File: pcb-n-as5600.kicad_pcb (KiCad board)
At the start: 2 copper layers, 41 x 35 mm, 26 parts, among them J1 Conn_01x04, J2 Conn_01x04_Pin, J5 Conn_01x04, J6 USB_C_Receptacle_USB2.0_14P, SW2 SW_Push, SW3 SW_Push, U4 AS5600, U5 STM32F103C8Tx, U6 AP2112K-3.3, Y2 8MHz

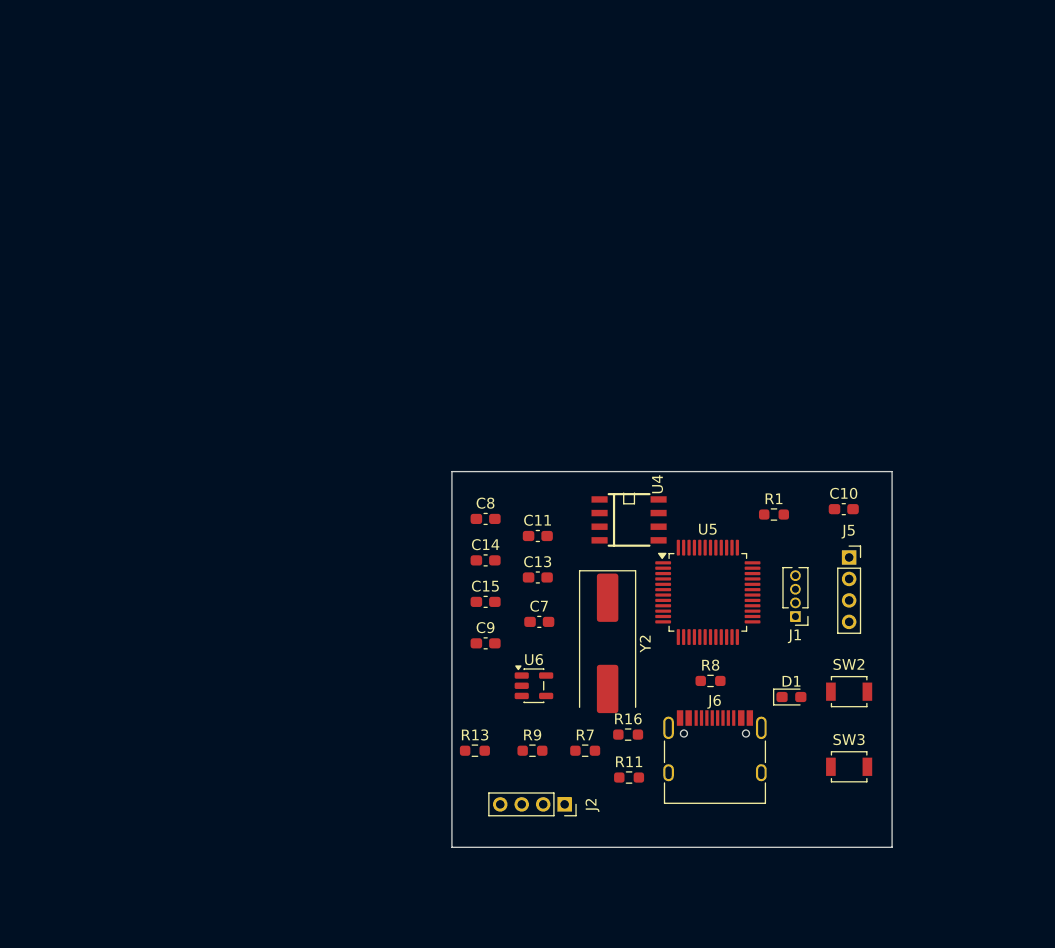
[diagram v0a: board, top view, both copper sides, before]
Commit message: changes to PCB, schematic
changed netlist, changed regulator used, changed PCB
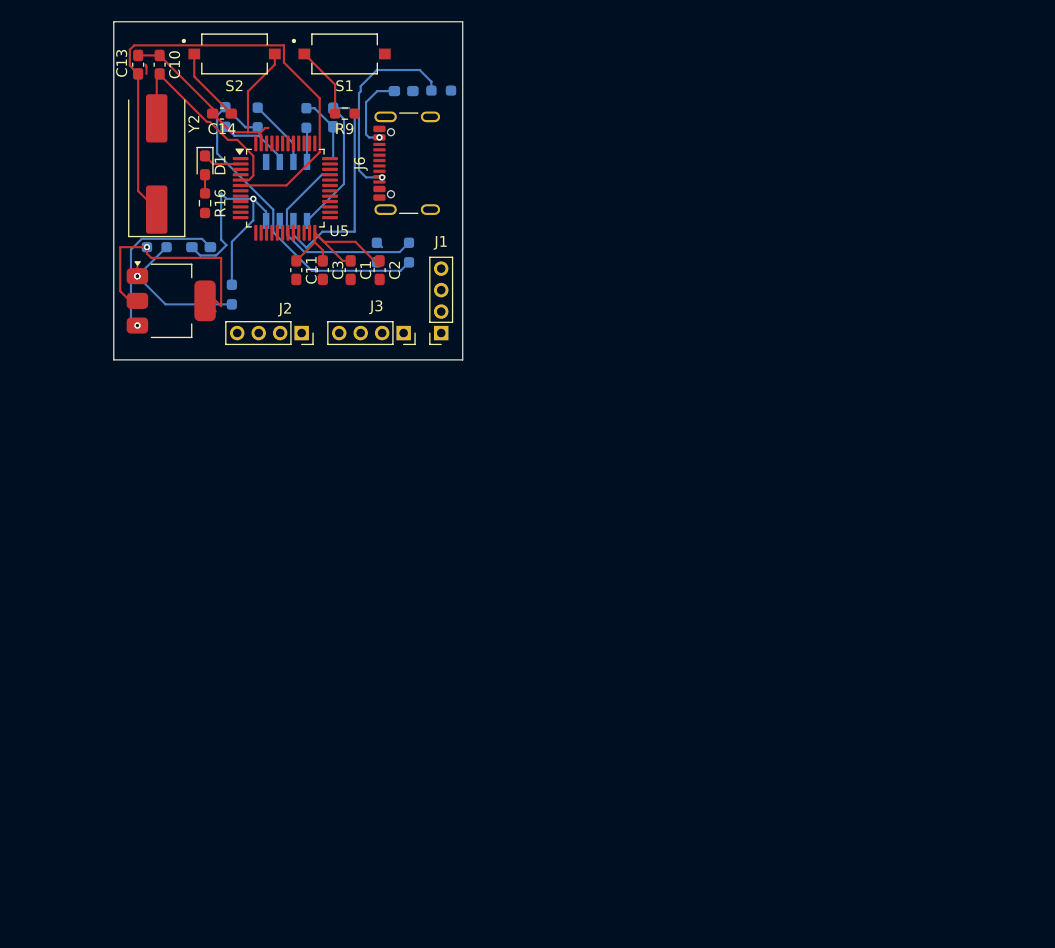
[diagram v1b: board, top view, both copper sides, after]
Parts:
- removed C15, C9: 100nF, Capacitor_SMD:C_0603_1608Metric_Pad1.08x0.95mm_HandSolder
- removed J5: Conn_01x04, Connector_PinSocket_2.00mm:PinSocket_1x04_P2.00mm_Vertical
- removed SW2, SW3: SW_Push, Button_Switch_SMD:SW_SPST_B3U-1000P
- removed U6: AP2112K-3.3, Package_TO_SOT_SMD:SOT-23-5
- added C1: 100nF, Capacitor_SMD:C_0603_1608Metric_Pad1.08x0.95mm_HandSolder, F.Cu at (126.1, 53.1)
- added C2: 100nF, Capacitor_SMD:C_0603_1608Metric_Pad1.08x0.95mm_HandSolder, F.Cu at (128.8, 53.1)
- added C3: 100nF, Capacitor_SMD:C_0603_1608Metric_Pad1.08x0.95mm_HandSolder, F.Cu at (123.5, 53.1)
- added C4: 100nF, Capacitor_SMD:C_0603_1608Metric_Pad1.08x0.95mm_HandSolder, B.Cu at (112.1, 51.0)
- added J3: Conn_01x04_Pin, Connector_PinSocket_2.00mm:PinSocket_1x04_P2.00mm_Vertical, F.Cu at (131.0, 59.0)
- added R2: 5k1, Resistor_SMD:R_0603_1608Metric_Pad0.98x0.95mm_HandSolder, B.Cu at (131.5, 51.5)
- added R3: 10k, Resistor_SMD:R_0603_1608Metric_Pad0.98x0.95mm_HandSolder, B.Cu at (115.0, 55.4)
- added R4: 10k, Resistor_SMD:R_0603_1608Metric_Pad0.98x0.95mm_HandSolder, B.Cu at (108.0, 51.0)
- added S1: TS09-63-25-WT-160-SMT-TR, TS09-63-25-WT-160-SMT-TR:SW_TS09-63-25-WT-160-SMT-TR, F.Cu at (125.5, 33.0)
- added S2: TS09-63-25-WT-160-SMT-TR, TS09-63-25-WT-160-SMT-TR:SW_TS09-63-25-WT-160-SMT-TR, F.Cu at (115.2, 33.0)
- added U1: AMS1117, Package_TO_SOT_SMD:SOT-223-3_TabPin2, F.Cu at (109.3, 56.0)
- C7, C8, R1, R11, R13, R7, R8, U4: moved to B.Cu
- J1: value Conn_01x04 -> Conn_01x04_Pin; footprint Connector_PinHeader_1.27mm:PinHeader_1x04_P1.27mm_Vertical -> Connector_PinSocket_2.00mm:PinSocket_1x04_P2.00mm_Vertical
- J6: footprint Connector_USB:USB_C_Receptacle_HRO_TYPE-C-31-M-12 -> Connector_USB:USB_C_Receptacle_GCT_USB4105-xx-A_16P_TopMnt_Horizontal
- moved C10 76.0 mm to (108.3, 34.0), turned to -90 degrees
- moved D1 73.7 mm to (112.5, 43.4), turned to -90 degrees
- moved R7 67.9 mm to (114.4, 38.9), turned to -90 degrees
- moved R11 66.3 mm to (134.5, 36.4), turned to 180 degrees
- moved R16 63.3 mm to (112.5, 46.9), turned to -90 degrees
- moved R13 62.4 mm to (117.4, 38.9), turned to 90 degrees
- moved J6 62.2 mm to (132.4, 43.2), turned to 90 degrees
- moved R9 61.9 mm to (125.5, 38.6)
- moved Y2 61.3 mm to (108.0, 43.2), turned to 90 degrees
- moved C13 60.6 mm to (106.3, 34.0), turned to -90 degrees
- moved R1 57.1 mm to (121.9, 39.0), turned to 90 degrees
- moved U5 54.5 mm to (120.0, 45.5)
- moved C7 50.8 mm to (124.4, 38.9), turned to -90 degrees
- moved R8 50.6 mm to (128.5, 51.5), turned to 90 degrees
- moved J2 50.3 mm to (121.5, 59.0)
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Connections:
- net /SCL renamed SCL
- net /SCLK renamed SCLK
- net /SDA renamed SDA
- net /SWDIO renamed SWDIO
- C10 pad 1: 3.3V -> GND
- C11 pad 1: 3.3V -> +3.3V
- C11 pad 2: VDD -> GND
- C13 pad 1: 3.3V -> GND
- C14 pad 1: 3.3V -> GND
- C7 pad 1: 3.3V -> +3.3V
- C7 pad 2: 3.3V -> GND
- C8 pad 1: 3.3V -> GND
- J1 pad 3: 3.3V -> /3.3V
- J1 pad 4: 3.3V -> GND
- J6 pad A1: 3.3V -> GND
- J6 pad A12: 3.3V -> GND
- J6 pad B1: 3.3V -> GND
- J6 pad B12: 3.3V -> GND
- R1 pad 2: 3.3V -> GND
- R11 pad 1: 3.3V -> GND
- R13 pad 1: 3.3V -> /3.3V
- R16 pad 2: 3.3V -> /3.3V
- R7 pad 1: 3.3V -> /3.3V
- R8 pad 1: 3.3V -> GND
- R9 pad 2: 3.3V -> +3.3V
- U4 pad 1: 3.3V -> +3.3V
- U4 pad 2: 3.3V -> +3.3V
- U4 pad 4: 3.3V -> GND
- U5 pad 1: unconnected-(U5-VBAT-Pad1) -> +3.3V
- U5 pad 23: 3.3V -> GND
- U5 pad 24: VDD -> +3.3V
- U5 pad 35: 3.3V -> GND
- U5 pad 36: VDD -> +3.3V
- U5 pad 47: 3.3V -> GND
- U5 pad 48: VDD -> +3.3V
- U5 pad 8: unconnected-(U5-VSSA-Pad8) -> GND
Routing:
- net +3.3V: track 0.00 -> 73.7 mm, vias 0 -> 1
- net GND: track 0.00 -> 54.7 mm, vias 0 -> 1
- net /OSC_OUT: track 0.00 -> 50.4 mm
- net /3.3V: track 0.00 -> 32.4 mm
- net MCU_D+: track 0.00 -> 20.1 mm
- net /OSC_IN: track 0.00 -> 19.4 mm
- net Net-(J6-CC1): track 0.00 -> 18.8 mm, vias 0 -> 1
- net +5V: track 0.00 -> 15.6 mm, vias 0 -> 1
- net Net-(U1-ADJ): track 0.00 -> 14.6 mm, vias 0 -> 2
- net Net-(C8-Pad2): track 0.00 -> 7.69 mm, vias 0 -> 1
- net NRST: track 0.00 -> 6.98 mm
- net BOOTO: track 0.00 -> 6.74 mm
- net SDA: track 0.00 -> 6.70 mm
- net SCL: track 0.00 -> 6.43 mm
- net LED: track 0.00 -> 3.63 mm
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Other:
- board size 41 x 35 mm -> 32.5 x 31.5 mm

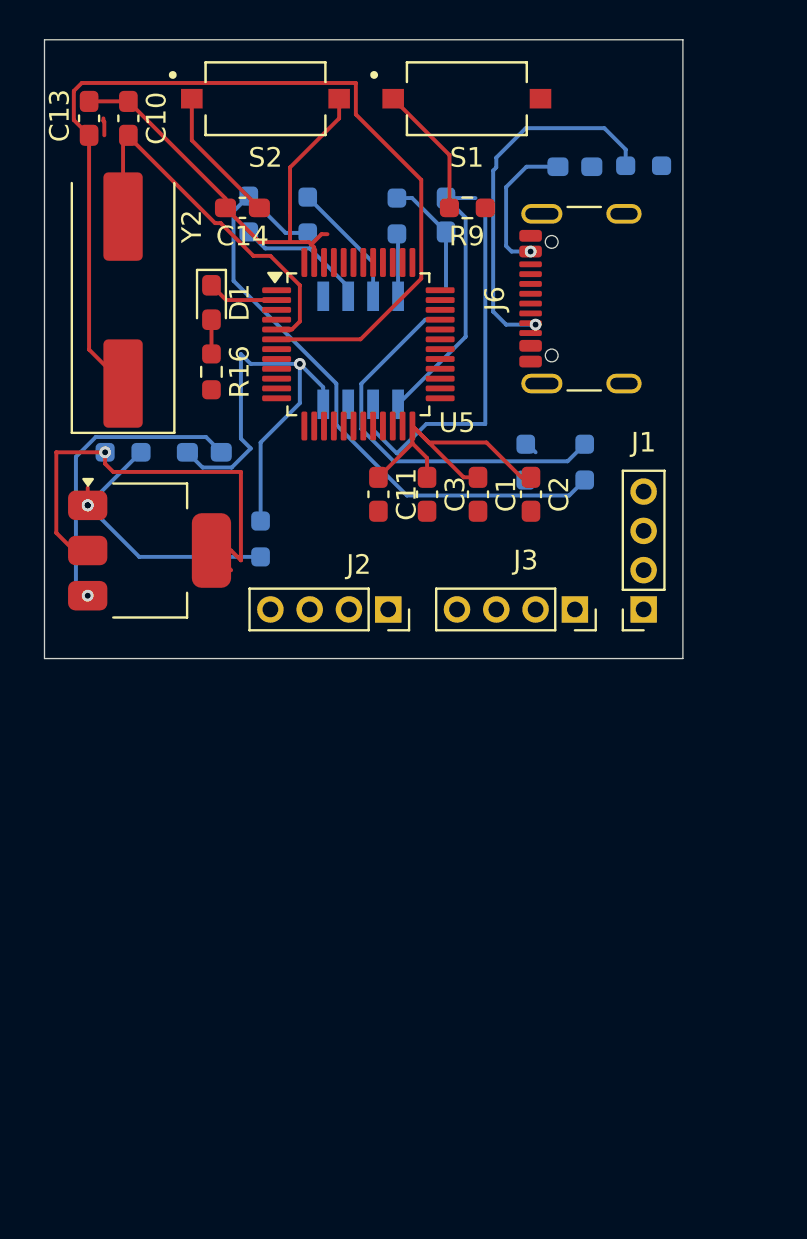
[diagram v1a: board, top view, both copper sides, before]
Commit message: iteration 3
better wiring, resisistors of devices on bottom instead
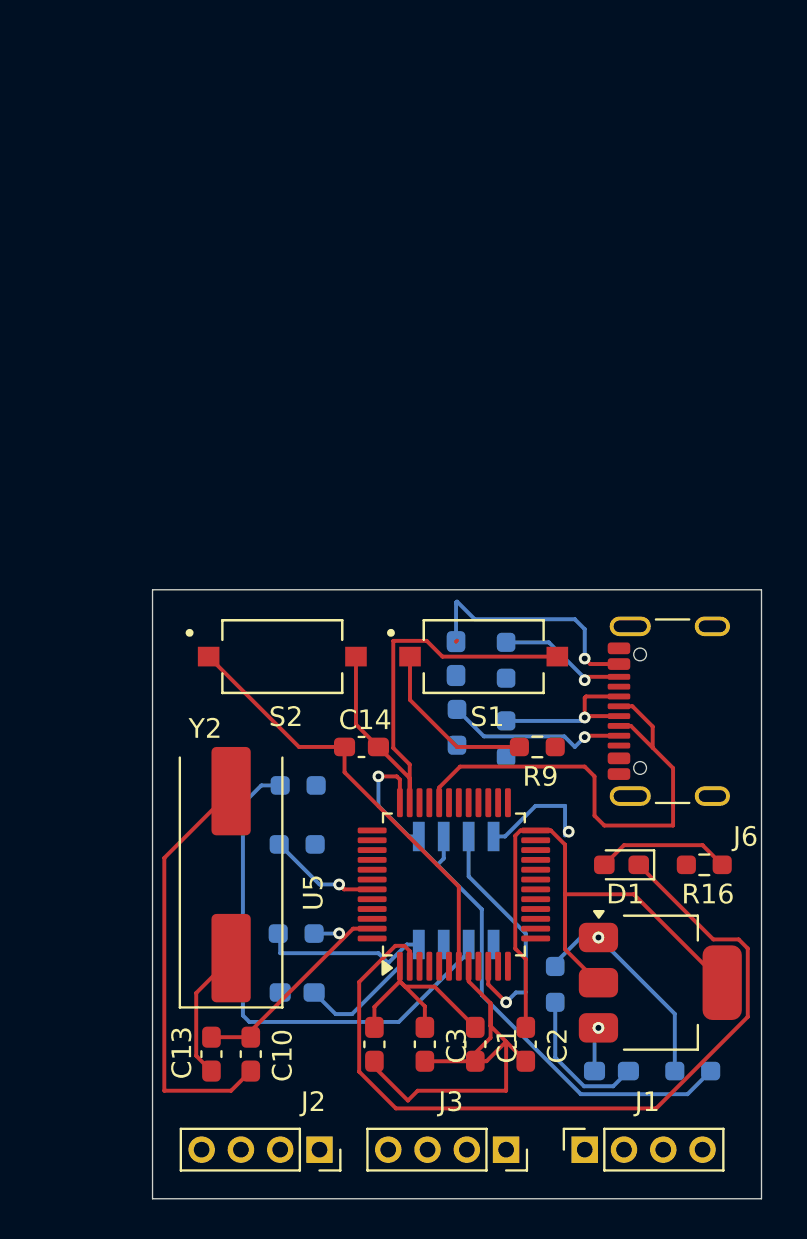
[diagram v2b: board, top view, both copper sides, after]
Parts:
- moved C10 48.0 mm to (114.5, 81.6)
- moved C13 48.0 mm to (112.5, 81.6)
- moved R4 42.8 mm to (137.0, 82.5), turned to 180 degrees
- moved C7 40.3 mm to (116.9, 78.5), turned to 180 degrees
- moved C4 37.7 mm to (132.9, 82.5), turned to 0 degrees
- moved R1 36.9 mm to (116.8, 75.5), turned to 0 degrees
- moved R16 35.5 mm to (137.6, 72.0), turned to 180 degrees
- moved D1 35.4 mm to (133.4, 72.0), turned to 180 degrees
- moved U1 34.1 mm to (135.3, 78.0)
- moved R13 32.0 mm to (116.9, 71.0), turned to 180 degrees
- moved R11 30.1 mm to (125.0, 65.0), turned to 90 degrees
- moved Y2 29.8 mm to (113.5, 72.5)
- moved R7 29.2 mm to (116.9, 68.0), turned to 180 degrees
- moved S1 28.4 mm to (126.4, 61.4)
- moved S2 28.4 mm to (116.1, 61.4)
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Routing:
- net /OSC_OUT: track 50.4 -> 6.81 mm
- net LED: track 3.63 -> 42.1 mm
- net /3.3V: track 32.4 -> 0.00 mm
- net MCU_D-: track 0.00 -> 25.3 mm
- net GND: track 54.7 -> 75.0 mm, vias 1 -> 2
- net SDA: track 6.70 -> 26.5 mm
- net NRST: track 6.98 -> 22.4 mm
- net +5V: track 15.6 -> 2.28 mm
- net /OUT: track 0.00 -> 12.6 mm, vias 0 -> 1
- net MCU_D+: track 20.1 -> 8.62 mm, vias 0 -> 1
- net Net-(J6-CC1): track 18.8 -> 9.27 mm
- net +3.3V: track 73.7 -> 79.9 mm
- net Net-(J6-CC2): track 0.67 -> 6.67 mm, vias 0 -> 1
- net Net-(U4-DIR): track 3.20 -> 8.69 mm
- net Net-(D1-A): track 1.74 -> 6.83 mm
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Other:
- board size 32.5 x 31.5 mm -> 31 x 31 mm
- board text added: "PCB Edge"

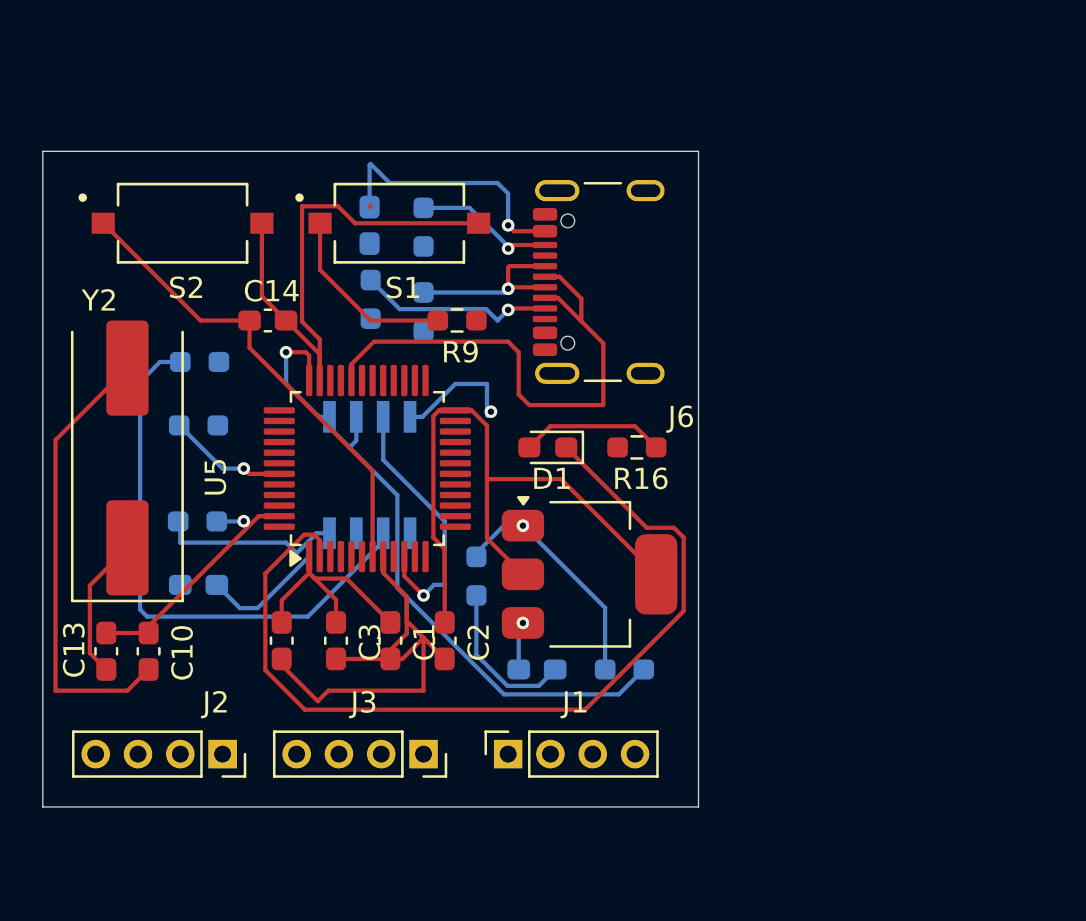
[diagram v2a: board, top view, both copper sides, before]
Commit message: changes toPCB
changed wiring, zones and position of the resistors and capacitors
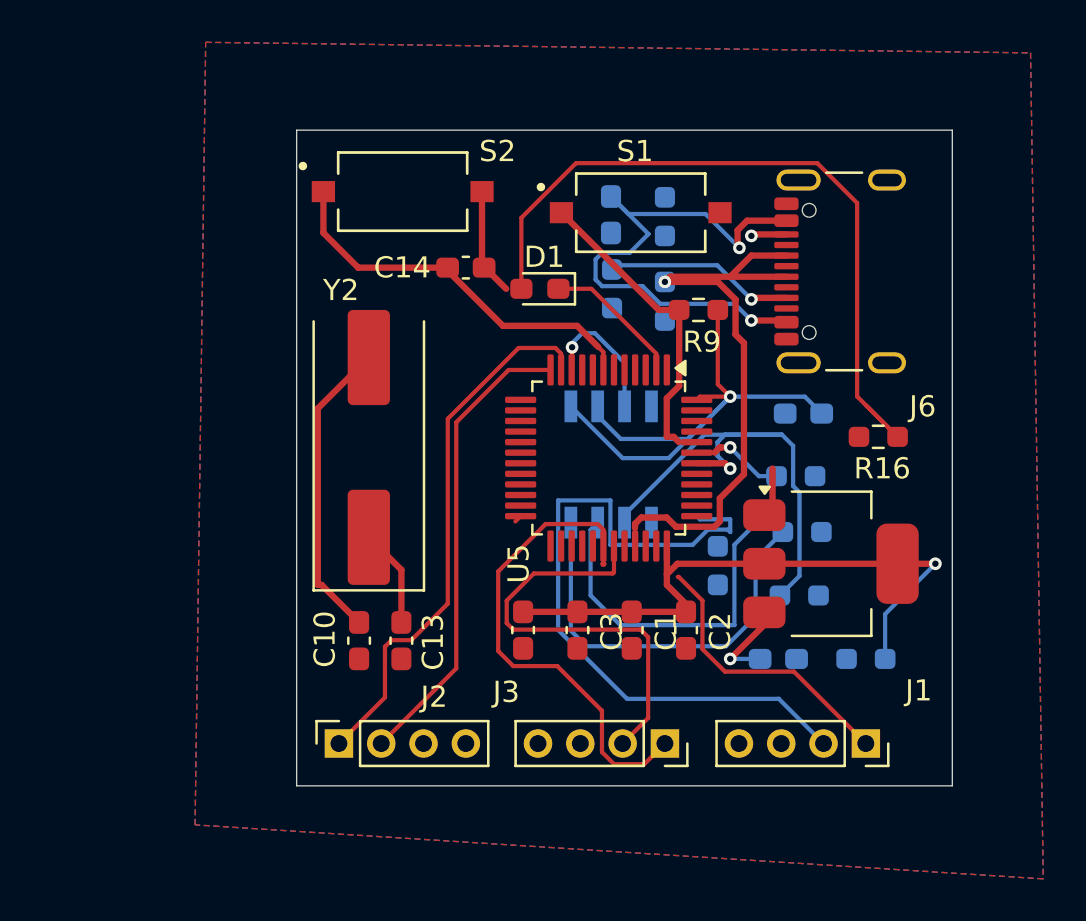
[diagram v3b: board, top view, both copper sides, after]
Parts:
- moved R7 30.4 mm to (145.3, 79.0)
- moved C7 29.7 mm to (145.5, 70.4)
- moved R1 28.6 mm to (145.4, 76.0)
- moved R13 28.3 mm to (145.1, 73.4)
- moved J1 16.9 mm to (148.4, 86.0), turned to -90 degrees
- moved C13 14.0 mm to (126.5, 81.1), turned to 90 degrees
- moved C1 11.4 mm to (137.3, 80.6)
- moved C3 11.4 mm to (134.8, 80.6)
- moved C8 11.4 mm to (136.4, 61.0)
- moved U4 11.4 mm to (136.4, 72.8)
- moved U5 11.4 mm to (136.3, 72.5), turned to -90 degrees
- moved C11 11.4 mm to (132.2, 80.6)
- moved C2 11.4 mm to (139.9, 80.6)
- moved C4 11.4 mm to (144.3, 82.0)
- moved J3 11.4 mm to (138.9, 86.0)
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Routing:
- net GND: track 75.0 -> 5.07 mm, vias 2 -> 0
- net LED: track 42.1 -> 6.67 mm
- net SCLK: track 0.00 -> 33.7 mm
- net Net-(D1-A): track 6.83 -> 35.1 mm
- net dum1: track 0.00 -> 25.7 mm
- net MCU_D-: track 25.3 -> 0.00 mm
- net /TX: track 0.00 -> 22.2 mm
- net dum2: track 0.00 -> 22.1 mm
- net +3.3V: track 79.9 -> 58.3 mm, vias 1 -> 2
- net /RX: track 0.00 -> 20.4 mm
- net MCU_D+: track 8.62 -> 28.4 mm
- net SCL: track 5.68 -> 22.3 mm
- net Net-(C8-Pad2): track 12.6 -> 26.8 mm, vias 1 -> 2
- net SWDIO: track 0.00 -> 13.5 mm
- net Net-(U4-DIR): track 8.69 -> 19.3 mm
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- added copper zone on B.Cu, net GND
- added copper zone on F.Cu, net GND
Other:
- board text removed: "PCB Edge"
